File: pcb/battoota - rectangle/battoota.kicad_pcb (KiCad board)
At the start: 2 copper layers, 123.9 x 90 mm, 38 parts

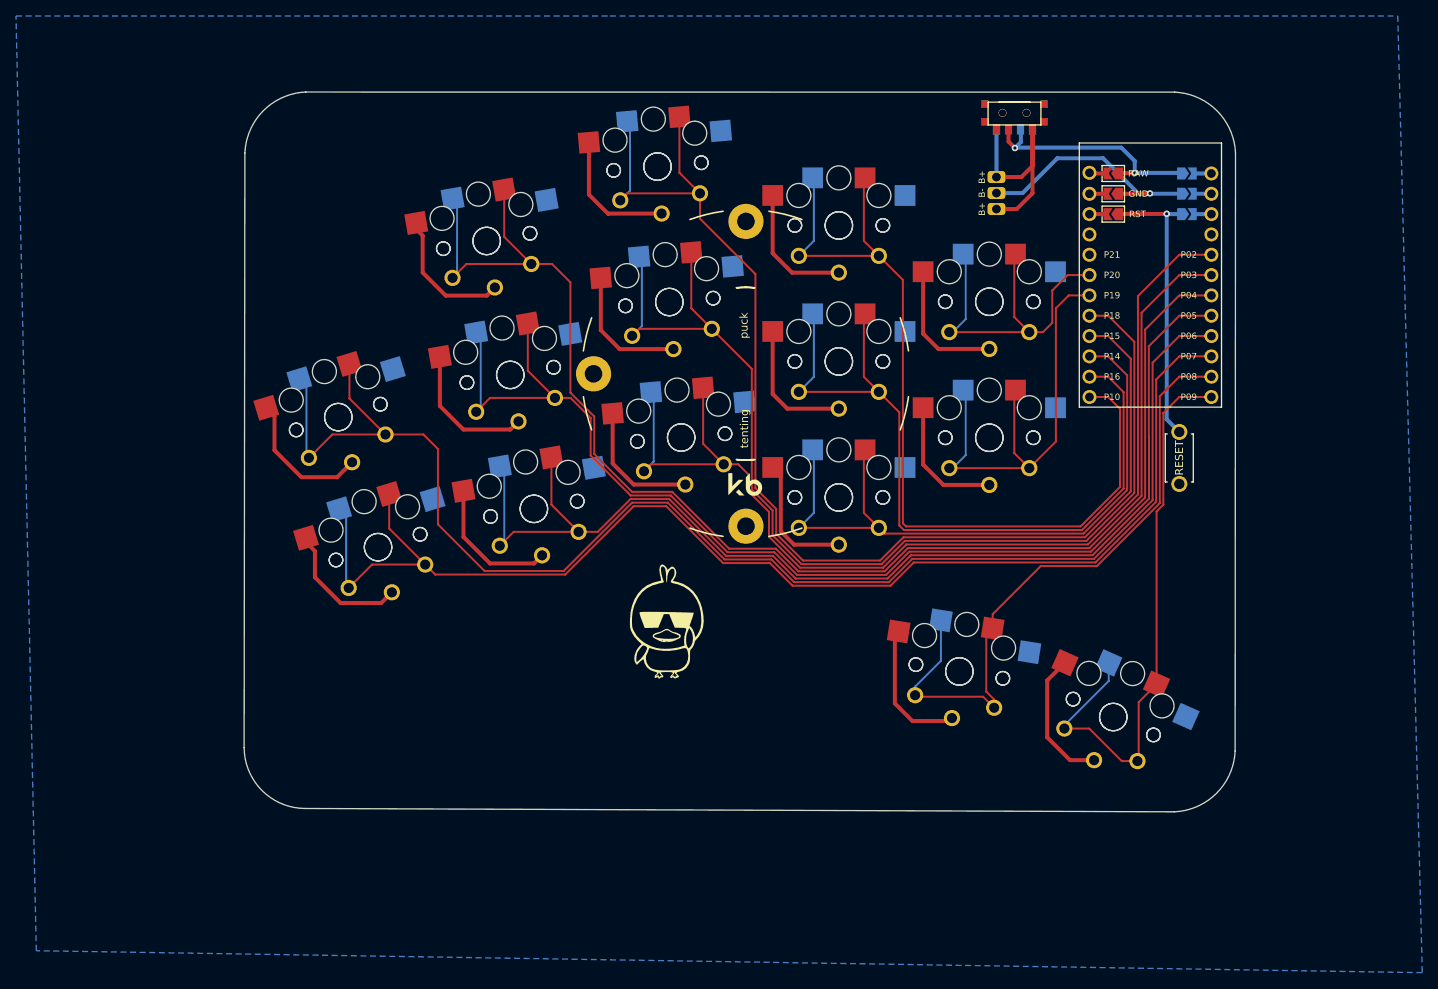
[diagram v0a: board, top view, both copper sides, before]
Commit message: more uniform rectangle for battoota
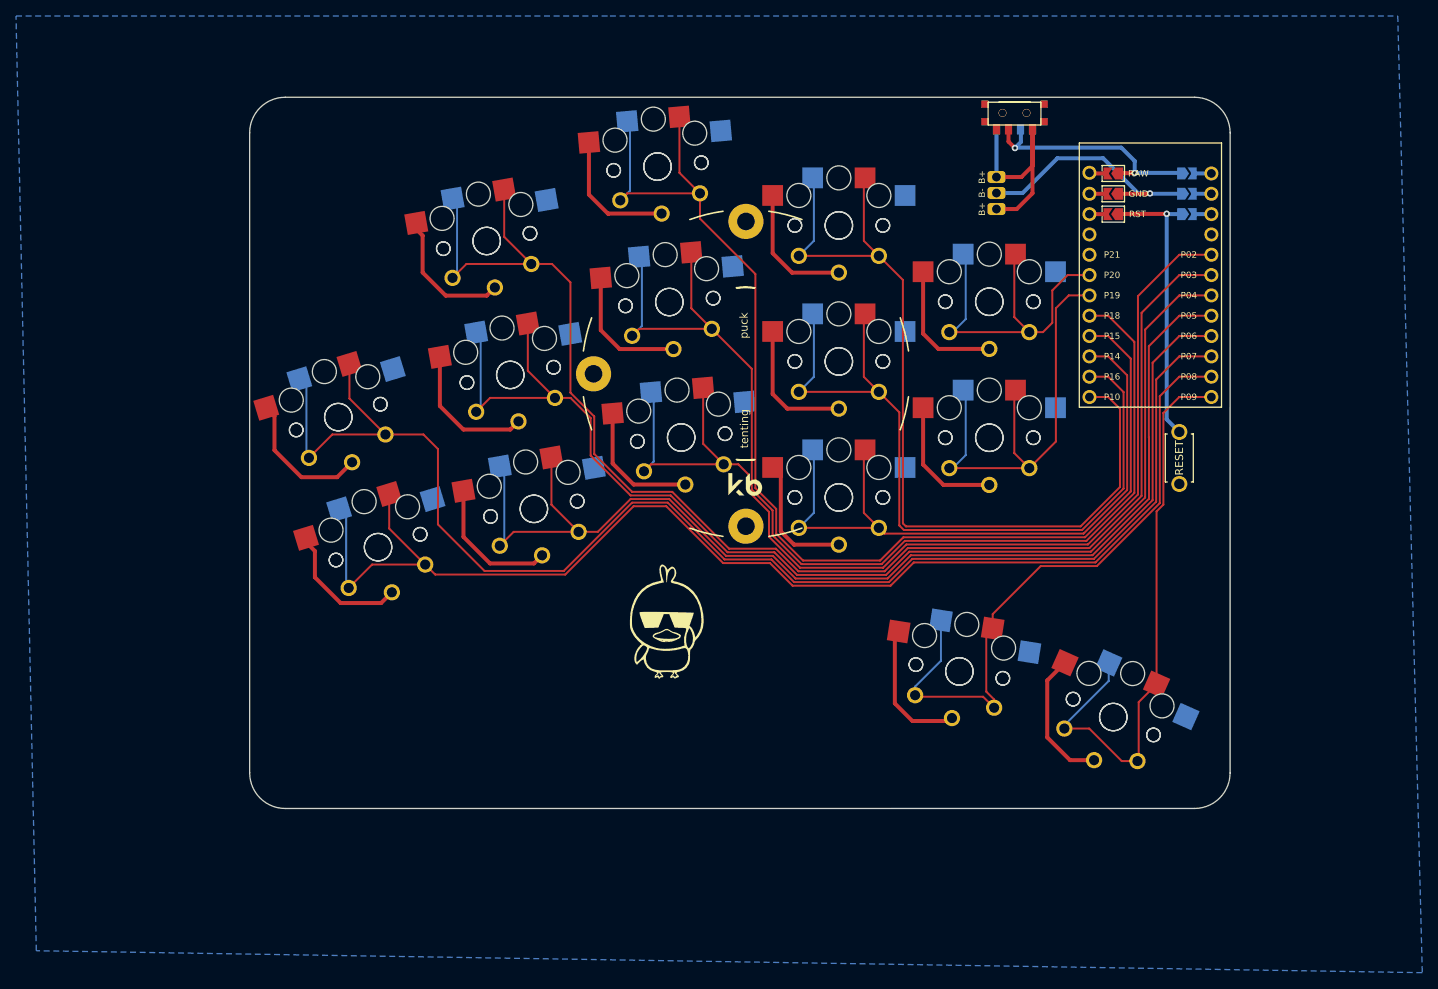
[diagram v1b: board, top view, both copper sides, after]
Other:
- board size 123.9 x 90 mm -> 122.6 x 88.9 mm
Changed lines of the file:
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@@
       ) (layer "B.SilkS") (width 0) (fill solid))
   )
-  (gr_line (start 157.373271 -123.349983) (end 48.779334 -123.36481) (layer "Edge.Cuts") (width 0.15))
-  (gr_arc (start 164.948263 -41.009332) (mid 162.628869 -35.71328) (end 157.334791 -33.389332) (layer "Edge.Cuts") (width 0.15))
-  (gr_line (start 41.165862 -115.74481) (end 41.071041 -41.428254) (layer "Edge.Cuts") (width 0.15))
-  (gr_arc (start 48.691041 -33.808254) (mid 43.311577 -36.04879) (end 41.071041 -41.428254) (layer "Edge.Cuts") (width 0.15))
-  (gr_line (start 164.948263 -41.009332) (end 164.993271 -115.736511) (layer "Edge.Cuts") (width 0.15))
-  (gr_line (start 157.334791 -33.389332) (end 48.691041 -33.808254) (layer "Edge.Cuts") (width 0.15))
-  (gr_arc (start 157.373271 -123.349983) (mid 162.669331 -121.030581) (end 164.993271 -115.736511) (layer "Edge.Cuts") (width 0.15))
-  (gr_arc (start 41.165862 -115.74481) (mid 43.485264 -121.04087) (end 48.779334 -123.36481) (layer "Edge.Cuts") (width 0.15))
+  (gr_line (start 164.316185 -38.254903) (end 164.319791 -118.263254) (layer "Edge.Cuts") (width 0.05))
+  (gr_arc (start 46.209791 -33.808254) (mid 43.066701 -35.110164) (end 41.764791 -38.253254) (layer "Edge.Cuts") (width 0.05))
+  (gr_arc (start 159.874791 -122.708254) (mid 163.017881 -121.406344) (end 164.319791 -118.263254) (layer "Edge.Cuts") (width 0.05))
+  (gr_line (start 46.209791 -33.808254) (end 159.871185 -33.809903) (layer "Edge.Cuts") (width 0.05))
+  (gr_line (start 41.761149 -118.266118) (end 41.764791 -38.253254) (layer "Edge.Cuts") (width 0.05))
+  (gr_line (start 159.874791 -122.708254) (end 46.206149 -122.711118) (layer "Edge.Cuts") (width 0.05))
+  (gr_arc (start 41.761149 -118.266118) (mid 43.063059 -121.409208) (end 46.206149 -122.711118) (layer "Edge.Cuts") (width 0.05))
+  (gr_arc (start 164.316185 -38.254903) (mid 163.014275 -35.111813) (end 159.871185 -33.809903) (layer "Edge.Cuts") (width 0.05))
   (segment (start 147.293059 -65.010791) (end 124.592825 -65.010791) (width 0.25) (layer "F.Cu") (net 1))
   (segment (start 124.592825 -65.010791) (end 121.686138 -62.104105) (width 0.25) (layer "F.Cu") (net 1))
